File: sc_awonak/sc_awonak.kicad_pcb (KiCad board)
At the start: 2 copper layers, 88.6 x 50.6 mm, 41 parts, among them J1 Conn_01x02, J2 Conn_01x02, J3 Analog Input, J4 Digital Input, J5 Analog Output

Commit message: More revision updates and add preview image
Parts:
- added J6: Conn_01x02, Connector_PinSocket_2.54mm:PinSocket_1x02_P2.54mm_Vertical, F.Cu at (108.9, 109.1)
- R11, R12, R13, R14: value 1K -> RLED
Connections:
- A1 pad VIN: unconnected-(A1-PadVIN) -> VIN
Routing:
- net VIN: track 0.00 -> 3.71 mm
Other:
- board text added: "+"
- board text added: "-"
- board text added: "5V"
- board text added: "ver0.1 2023-12-18"
- board text removed: "ver0.1 2023-12-17"

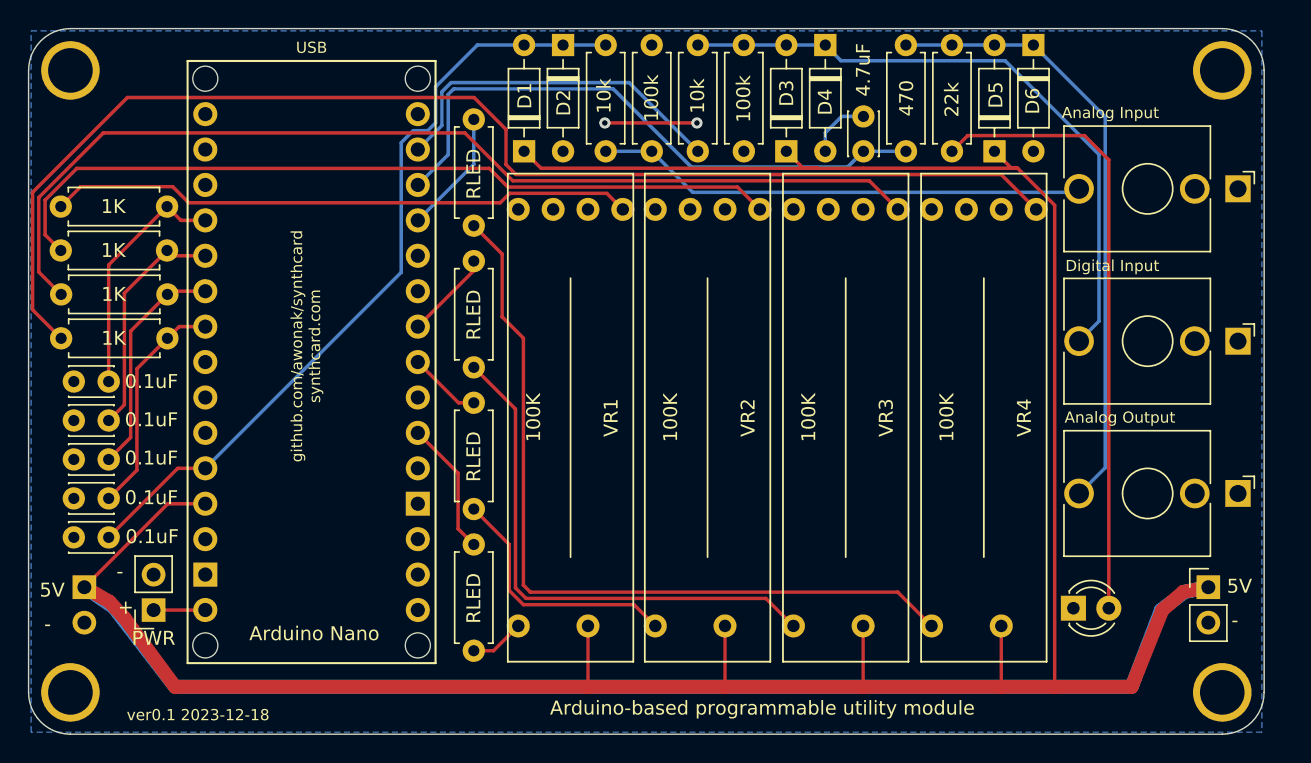
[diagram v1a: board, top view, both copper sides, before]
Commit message: Added 3d rendering, schematic PDF, and more pcb revisions.
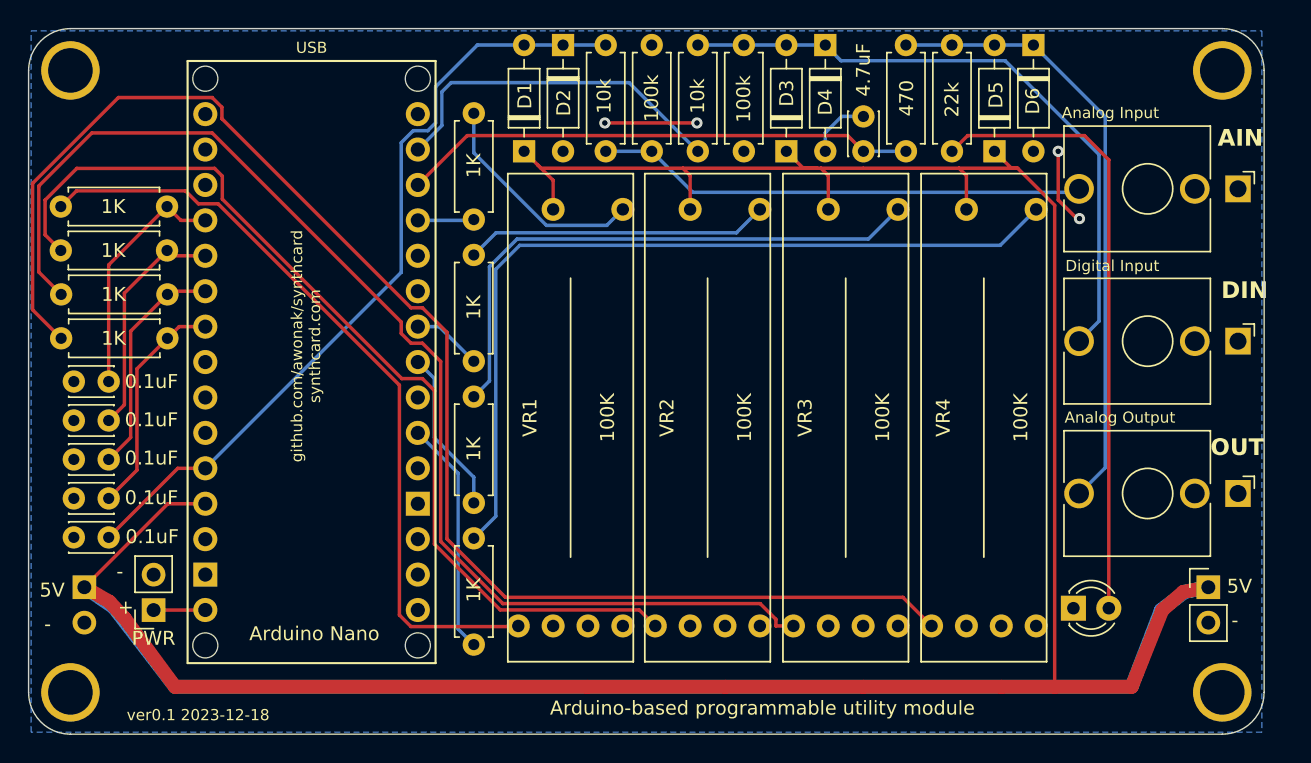
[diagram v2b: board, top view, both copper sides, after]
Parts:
- R11, R12, R13, R14: value RLED -> 1K
- moved R11 38.5 mm to (131.8, 73.5), turned to -90 degrees
- moved R14 22.4 mm to (131.8, 104.0), turned to -90 degrees
- moved R12 18.2 mm to (131.8, 83.6), turned to -90 degrees
- moved R13 2.10 mm to (131.8, 93.8), turned to -90 degrees
- turned VR1 to 0 degrees
- turned VR2 to 0 degrees
- turned VR3 to 0 degrees
- turned VR4 to 0 degrees
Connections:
- R11 pad 2: D3 -> D9
- R12 pad 2: D5 -> D6
- R13 pad 2: D6 -> D5
- R14 pad 2: D9 -> D3
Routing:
- net Net-(VR1B-2): track 42.1 -> 55.9 mm
- net Net-(VR3B-2): track 73.4 -> 87.1 mm
- net Net-(VR4B-2): track 90.9 -> 103.8 mm
- net Net-(VR2B-2): track 57.5 -> 69.8 mm
- net Net-(VR1A-A): track 3.93 -> 16.2 mm
- net D3: track 9.66 -> 16.8 mm
- net D5: track 5.22 -> 11.8 mm
- net D10: track 43.2 -> 36.9 mm
- net D9: track 8.90 -> 4.04 mm
- net +5V: track 285.8 -> 281.4 mm
- net GND: track 14.2 -> 18.4 mm, vias 2 -> 4
- net Net-(VR2A-A): track 18.4 -> 21.9 mm
- net Net-(VR4A-A): track 57.7 -> 60.5 mm
- net Net-(VR3A-A): track 38.1 -> 40.8 mm
- net D6: track 6.36 -> 5.04 mm
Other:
- board text added: "AIN"
- board text added: "DIN"
- board text added: "OUT"

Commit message: Add ibom and update gitignore
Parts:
- D1, D2, D3, D4, D5, D6: value 1N4148 -> BAT43
- renumbered J3 to J1, J4 to J2, J5 to J3, J2 to J4, J1 to J5
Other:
- board text added: "ver0.2 2023-12-19"
- board text removed: "ver0.1 2023-12-18"
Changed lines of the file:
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@@
   (net 35 "+5V")
   (net 36 "Net-(D7-A)")
-  (net 37 "Net-(J3-PadT)")
-  (net 38 "unconnected-(J4-PadTN)")
-  (net 39 "unconnected-(J5-PadTN)")
+  (net 37 "Net-(J1-PadT)")
+  (net 38 "unconnected-(J1-PadTN)")
+  (net 39 "unconnected-(J2-PadTN)")
   (net 40 "Net-(VR1A-A)")
   (net 41 "Net-(VR2A-A)")
@@
         (effects (font (size 1 1) (thickness 0.15)))
     )
-    (fp_text value "1N4148" (at 3.81 2.12 90) (layer "F.Fab") hide
+    (fp_text value "BAT43" (at 3.81 2.12 90) (layer "F.Fab") hide
         (effects (font (size 1 1) (thickness 0.15)))
     )
@@
       (stroke (width 0.1) (type solid)) (layer "F.Fab"))
     (pad "1" thru_hole circle (at 0 0 90) (size 1.6 1.6) (drill 0.8) (layers "*.Cu" "*.Mask")
-      (net 37 "Net-(J3-PadT)") (pintype "passive"))
+      (net 37 "Net-(J1-PadT)") (pintype "passive"))
     (pad "2" thru_hole oval (at 7.62 0 90) (size 1.6 1.6) (drill 0.8) (layers "*.Cu" "*.Mask")
       (net 1 "GND") (pintype "passive"))
@@
     (property "Sheetfile" "sc_awonak.kicad_sch")
     (property "Sheetname" "")
+    (property "exclude_from_bom" "")
     (property "ki_description" "Mounting Hole with connection")
     (property "ki_keywords" "mounting hole")
-    (attr exclude_from_pos_files)
+    (attr exclude_from_pos_files exclude_from_bom)
     (fp_text reference "H4" (at 0 -4.2) (layer "F.SilkS") hide
         (effects (font (size 1 1) (thickness 0.15)))
@@
         (effects (font (size 1 1) (thickness 0.15)))
     )
-    (fp_text value "1N4148" (at 3.81 2.12 90) (layer "F.Fab") hide
+    (fp_text value "BAT43" (at 3.81 2.12 90) (layer "F.Fab") hide
         (effects (font (size 1 1) (thickness 0.15)))
     )
@@
       (stroke (width 0.1) (type solid)) (layer "F.Fab"))
     (pad "1" thru_hole circle (at 0 0 90) (size 1.6 1.6) (drill 0.8) (layers "*.Cu" "*.Mask")
-      (net 37 "Net-(J3-PadT)") (pintype "passive"))
+      (net 37 "Net-(J1-PadT)") (pintype "passive"))
     (pad "2" thru_hole oval (at 7.62 0 90) (size 1.6 1.6) (drill 0.8) (layers "*.Cu" "*.Mask")
       (net 2 "A7") (pintype "passive"))
@@
     (property "Sheetfile" "sc_awonak.kicad_sch")
     (property "Sheetname" "")
+    (property "exclude_from_bom" "")
     (property "ki_description" "Mounting Hole with connection")
     (property "ki_keywords" "mounting hole")
-    (attr exclude_from_pos_files)
+    (attr exclude_from_pos_files exclude_from_bom)
     (fp_text reference "H2" (at 0 -4.2) (layer "F.SilkS") hide
         (effects (font (size 1 1) (thickness 0.15)))
@@
     (property "ki_keywords" "audio jack receptacle mono headphones phone TS connector")
     (attr through_hole)
-    (fp_text reference "J3" (at -4.03 1.08 90) (layer "F.Fab")
+    (fp_text reference "J1" (at -4.03 1.08 90) (layer "F.Fab")
         (effects (font (size 1 1) (thickness 0.15)))
     )
@@
       (net 1 "GND") (pintype "passive"))
     (pad "T" thru_hole circle (at 0 11.4 90) (size 2.13 2.13) (drill 1.43) (layers "*.Cu" "*.Mask")
-      (net 37 "Net-(J3-PadT)") (pintype "passive"))
+      (net 37 "Net-(J1-PadT)") (pintype "passive"))
     (pad "TN" thru_hole circle (at 0 3.1 90) (size 2.13 2.13) (drill 1.42) (layers "*.Cu" "*.Mask")
-      (net 30 "unconnected-(J3-PadTN)") (pintype "passive+no_connect"))
+      (net 38 "unconnected-(J1-PadTN)") (pintype "passive+no_connect"))
     (zone (net 0) (net_name "") (layer "F.Cu") (hatch full 0.508)
       (connect_pads (clearance 0))
@@
     (property "Sheetfile" "sc_awonak.kicad_sch")
     (property "Sheetname" "")
+    (property "exclude_from_bom" "")
     (property "ki_description" "Mounting Hole with connection")
     (property "ki_keywords" "mounting hole")
-    (attr exclude_from_pos_files)
+    (attr exclude_from_pos_files exclude_from_bom)
     (fp_text reference "H1" (at 0 -4.2) (layer "F.SilkS") hide
         (effects (font (size 1 1) (thickness 0.15)))
@@
     (property "Sheetfile" "sc_awonak.kicad_sch")
     (property "Sheetname" "")
+    (property "exclude_from_bom" "")
     (property "ki_description" "Generic connector, single row, 01x02, script generated (kicad-library-utils/schlib/autogen/connector/)")
     (property "ki_keywords" "connector")
-    (attr through_hole)
-    (fp_text reference "J2" (at 0 -2.33) (layer "F.SilkS") hide
+    (attr through_hole exclude_from_bom)
+    (fp_text reference "J4" (at 0 -2.33) (layer "F.SilkS") hide
         (effects (font (size 1 1) (thickness 0.15)))
     )
@@
         (effects (font (size 1 1) (thickness 0.15)))
     )
-    (fp_text value "1N4148" (at 3.81 2.12 90) (layer "F.Fab") hide
+    (fp_text value "BAT43" (at 3.81 2.12 90) (layer "F.Fab") hide
         (effects (font (size 1 1) (thickness 0.15)))
     )
@@
         (effects (font (size 1 1) (thickness 0.15)))
     )
-    (fp_text value "1N4148" (at 3.81 2.12 90) (layer "F.Fab") hide
+    (fp_text value "BAT43" (at 3.81 2.12 90) (layer "F.Fab") hide
         (effects (font (size 1 1) (thickness 0.15)))
     )
@@
     (property "Sheetfile" "sc_awonak.kicad_sch")
     (property "Sheetname" "")
+    (property "exclude_from_bom" "")
     (property "ki_description" "Generic connector, single row, 01x02, script generated (kicad-library-utils/schlib/autogen/connector/)")
     (property "ki_keywords" "connector")
-    (attr through_hole)
+    (attr through_hole exclude_from_bom)
     (fp_text reference "J6" (at 0 -2.77 180) (layer "F.SilkS") hide
         (effects (font (size 1 1) (thickness 0.15)))
@@
     (property "Sheetfile" "sc_awonak.kicad_sch")
     (property "Sheetname" "")
+    (property "exclude_from_bom" "")
     (property "ki_description" "Mounting Hole with connection")
     (property "ki_keywords" "mounting hole")
-    (attr exclude_from_pos_files)
+    (attr exclude_from_pos_files exclude_from_bom)
     (fp_text reference "H3" (at 0 -4.2) (layer "F.SilkS") hide
         (effects (font (size 1 1) (thickness 0.15)))
@@
         (effects (font (size 1 1) (thickness 0.15)))
     )
-    (fp_text value "1N4148" (at 3.81 2.12 90) (layer "F.Fab") hide
+    (fp_text value "BAT43" (at 3.81 2.12 90) (layer "F.Fab") hide
         (effects (font (size 1 1) (thickness 0.15)))
     )
@@
         (effects (font (size 1 1) (thickness 0.15)))
     )
-    (fp_text value "1N4148" (at 3.81 2.12 90) (layer "F.Fab") hide
+    (fp_text value "BAT43" (at 3.81 2.12 90) (layer "F.Fab") hide
         (effects (font (size 1 1) (thickness 0.15)))
     )
@@
     (property "ki_keywords" "audio jack receptacle mono headphones phone TS connector")
     (attr through_hole)
-    (fp_text reference "J4" (at -4.03 1.08 90) (layer "F.Fab")
+    (fp_text reference "J2" (at -4.03 1.08 90) (layer "F.Fab")
         (effects (font (size 1 1) (thickness 0.15)))
     )
@@
       (net 19 "Net-(D3-A)") (pintype "passive"))
     (pad "TN" thru_hole circle (at 0 3.1 90) (size 2.13 2.13) (drill 1.42) (layers "*.Cu" "*.Mask")
-      (net 38 "unconnected-(J4-PadTN)") (pintype "passive+no_connect"))
+      (net 39 "unconnected-(J2-PadTN)") (pintype "passive+no_connect"))
     (zone (net 0) (net_name "") (layer "F.Cu") (hatch full 0.508)
       (connect_pads (clearance 0))
@@
     (property "ki_keywords" "audio jack receptacle mono headphones phone TS connector")
     (attr through_hole)
-    (fp_text reference "J5" (at -4.03 1.08 90) (layer "F.Fab")
+    (fp_text reference "J3" (at -4.03 1.08 90) (layer "F.Fab")
         (effects (font (size 1 1) (thickness 0.15)))
     )
@@
       (net 25 "Net-(D5-A)") (pintype "passive"))
     (pad "TN" thru_hole circle (at 0 3.1 90) (size 2.13 2.13) (drill 1.42) (layers "*.Cu" "*.Mask")
-      (net 39 "unconnected-(J5-PadTN)") (pintype "passive+no_connect"))
+      (net 30 "unconnected-(J3-PadTN)") (pintype "passive+no_connect"))
     (zone (net 0) (net_name "") (layer "F.Cu") (hatch full 0.508)
       (connect_pads (clearance 0))
@@
     (property "Sheetfile" "sc_awonak.kicad_sch")
     (property "Sheetname" "")
+    (property "exclude_from_bom" "")
     (property "ki_description" "Generic connector, single row, 01x02, script generated (kicad-library-utils/schlib/autogen/connector/)")
     (property "ki_keywords" "connector")
-    (attr through_hole)
-    (fp_text reference "J1" (at 0 2.33) (layer "B.SilkS") hide
+    (attr through_hole exclude_from_bom)
+    (fp_text reference "J5" (at 0 2.33) (layer "B.SilkS") hide
         (effects (font (size 1 1) (thickness 0.15)) (justify mirror))
     )
@@
     (effects (font (size 1 1) (thickness 0.15)) (justify left bottom))
   )
-  (gr_text "ver0.1 2023-12-18" (at 106.934 117.094) (layer "F.SilkS")
+  (gr_text "ver0.2 2023-12-19" (at 106.934 117.094) (layer "F.SilkS")
     (effects (font (size 0.8 0.8) (thickness 0.15)) (justify left bottom))
   )

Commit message: hardware revision ver0.2
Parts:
- added G***: LOGO, Demo:socials, F.Cu at (119.0, 97.6)
- C1: value 0.1uF -> C1
- C2: value 0.1uF -> C2
- C3: value 0.1uF -> C3
- C4: value 0.1uF -> C4
- C5: value 0.1uF -> C5
- C6: value 4.7uF -> C6
- moved C6 12.4 mm to (172.0, 74.1)
- moved D5 9.40 mm to (159.8, 76.2)
- moved D6 9.40 mm to (162.6, 68.6)
- moved R10 6.10 mm to (168.9, 68.6)
- moved D7 0.94 mm to (175.8, 109.0)
- moved R9 0.51 mm to (165.6, 68.6)
- moved VR1 0.08 mm to (138.7, 95.3)
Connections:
- C6 pad 1: D10 -> Net-(C6-Pad1)
- D5 pad 2: Net-(D5-A) -> D10
- D6 pad 1: Net-(D5-A) -> D10
- J3 pad T: Net-(D5-A) -> Net-(C6-Pad1)
- R10 pad 1: Net-(D5-A) -> D10
- R10 pad 2: D10 -> Net-(C6-Pad1)
- R9 pad 1: Net-(D5-A) -> D10
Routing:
- net Net-(D5-A): track 44.2 -> 0.00 mm
- net Net-(C6-Pad1): track 0.00 -> 36.3 mm
- net D10: track 36.9 -> 45.3 mm
- net GND: track 18.4 -> 13.8 mm
- net Net-(D7-A): track 44.6 -> 46.8 mm
- net Net-(D3-A): track 46.0 -> 47.4 mm
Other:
- board text added: "Arduino-based programmable eurorack utility module"
- board text added: "ver0.2 2023-12-28"
- board text removed: "Arduino-based programmable utility module"
- board text removed: "github.com/awonak/synthcard synthcard.com"
- board text removed: "ver0.2 2023-12-19"

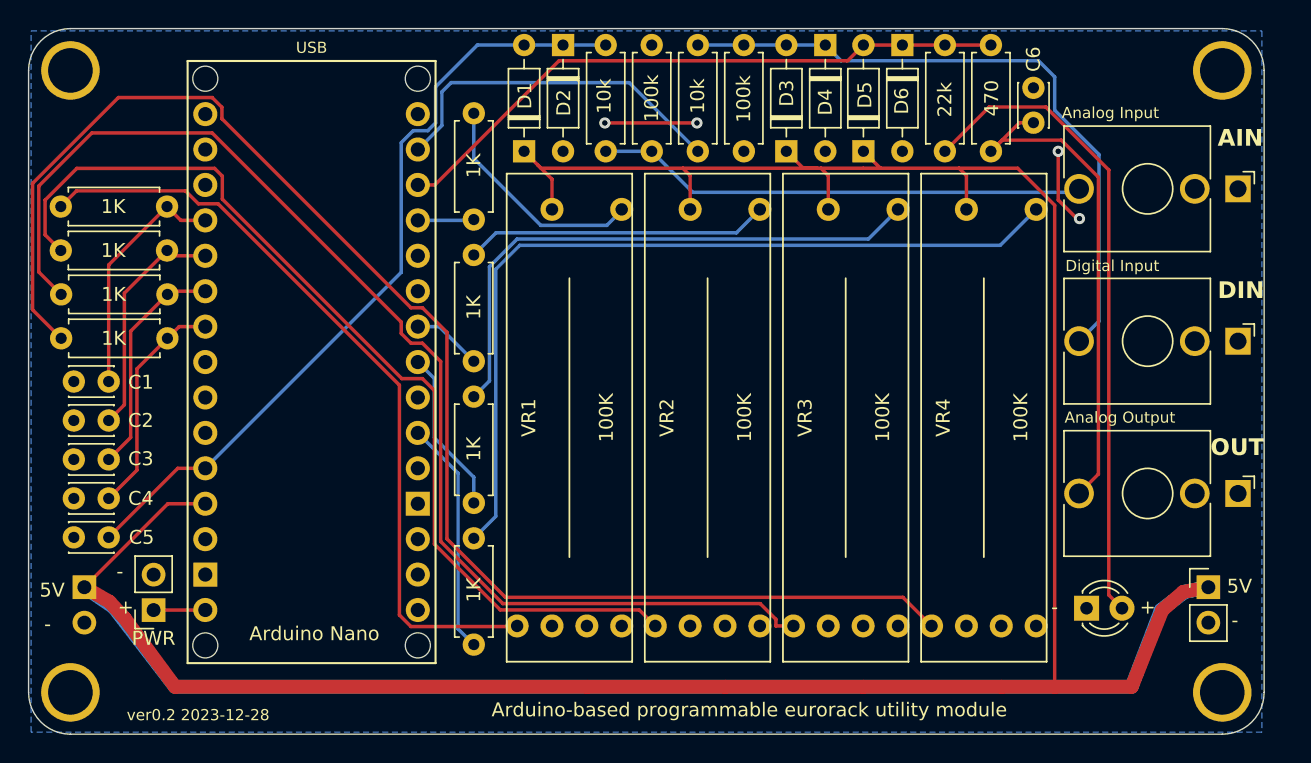
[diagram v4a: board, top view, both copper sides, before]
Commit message: update a few silkscreen details. larger 5v trace. update ibom.
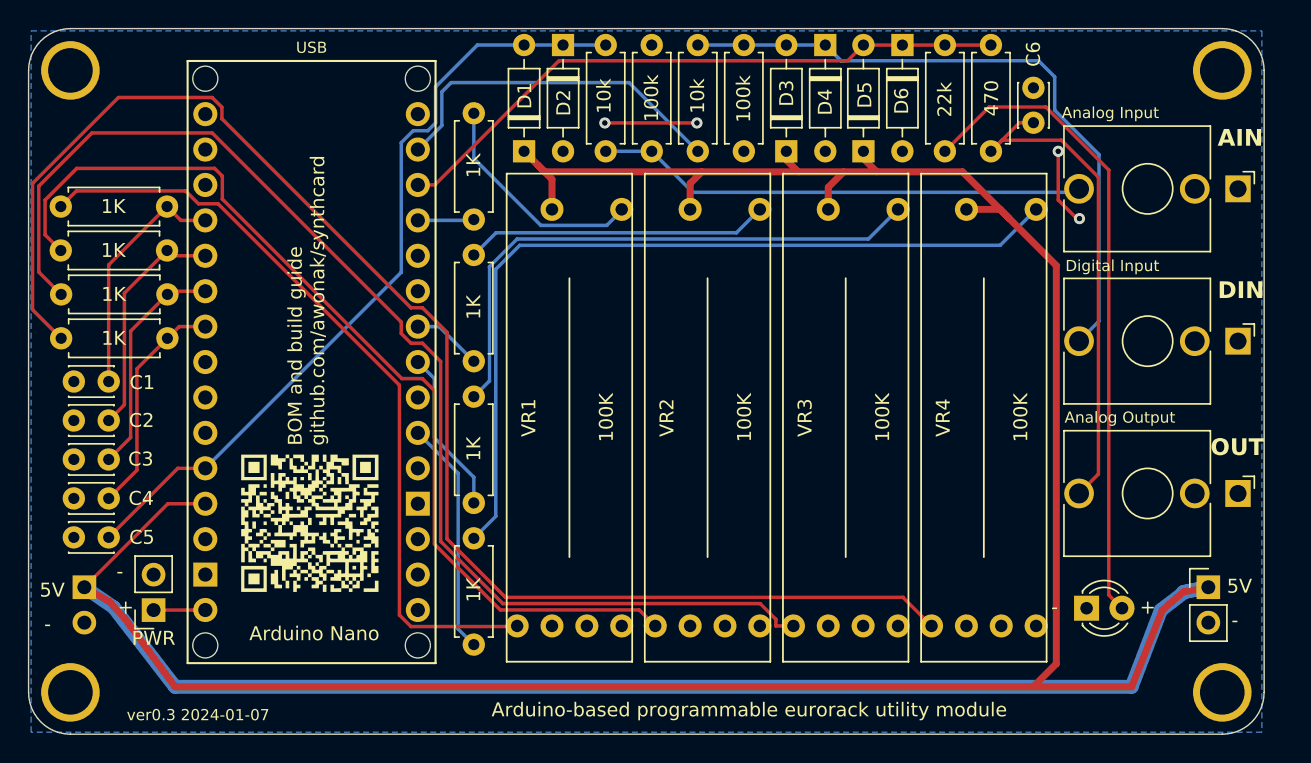
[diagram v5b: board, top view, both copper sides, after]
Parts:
- added G***: LOGO, Demo:qr, F.Cu at (120.0, 77.5)
- added G***: LOGO, Demo:qr2, F.Cu at (120.1, 102.9)
- C1: value C1 -> 0.1uF
- C2: value C2 -> 0.1uF
- C3: value C3 -> 0.1uF
- C4: value C4 -> 0.1uF
- C5: value C5 -> 0.1uF
- C6: value C6 -> 4.7uF
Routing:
- net +5V: track 281.0 -> 278.0 mm
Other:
- board text added: "BOM and build guide github.com/awonak/synthcard"
- board text added: "Software Engineer adam.wonak@gmail.com github.com/awonak/synthcard synthcard.com"
- board text added: "ver0.3 2024-01-07"
- board text removed: "Software Engineer adam.wonak@gmail.com github.com/awonak synthcard.com"
- board text removed: "ver0.2 2023-12-28"
